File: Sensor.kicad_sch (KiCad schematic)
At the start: 28 parts

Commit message: Add IOT Part
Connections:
- net SPI1_SCLK renamed SPI1_SCK
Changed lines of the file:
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@@
 		)
 	)
-	(label "SPI1_SCLK"
+	(label "SPI1_SCK"
 		(at 163.83 57.15 0)
 		(effects
@@
 		)
 	)
-	(label "SPI1_SCLK"
+	(label "SPI1_SCK"
 		(at 26.67 55.88 0)
 		(effects
@@
 		)
 	)
-	(label "SPI1_SCLK"
+	(label "SPI1_SCK"
 		(at 191.77 135.89 0)
 		(effects

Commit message: IoT part finalization
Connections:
- net SPI1_MISO: no longer U?.1 (SDO/SA0)
- net SPI1_MOSI: no longer U?.14 (SDA)
- net SPI1_SCK: no longer U?.13 (SCL)
- net I2C1_SCL renamed I2C2_SCL
- net I2C1_SDA renamed I2C2_SDA
- new net SPI2_MISO: U?.1 (SDO/SA0)
- new net SPI2_MOSI: U?.14 (SDA)
- new net SPI2_SCK: U?.13 (SCL)

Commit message: IOT part Finilization
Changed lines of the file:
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@@
 	)
 	(junction
-		(at 48.26 35.56)
+		(at 46.99 44.45)
 		(diameter 0)
 		(color 0 0 0 0)
@@
 	)
 	(bus_entry
-		(at 48.26 46.99)
+		(at 46.99 55.88)
 		(size -2.54 2.54)
 		(stroke
 			(width 0)
 			(type default)
+			(color 0 0 132 1)
 		)
 	)
 	(bus_entry
-		(at 48.26 49.53)
+		(at 46.99 58.42)
 		(size 2.54 2.54)
 		(stroke
 			(width 0)
 			(type default)
+			(color 0 0 132 1)
 		)
 	)
 	(bus_entry
-		(at 48.26 54.61)
+		(at 46.99 63.5)
 		(size -2.54 2.54)
 		(stroke
 			(width 0)
 			(type default)
+			(color 0 0 132 1)
 		)
 	)
 	(bus_entry
-		(at 48.26 46.99)
+		(at 46.99 55.88)
 		(size 2.54 2.54)
 		(stroke
 			(width 0)
 			(type default)
+			(color 0 0 132 1)
 		)
 	)
 	(bus_entry
-		(at 48.26 40.64)
+		(at 46.99 49.53)
 		(size -2.54 2.54)
 		(stroke
 			(width 0)
 			(type default)
+			(color 0 0 132 1)
 		)
 	)
 	(bus_entry
-		(at 48.26 52.07)
+		(at 46.99 60.96)
 		(size 2.54 2.54)
 		(stroke
 			(width 0)
 			(type default)
+			(color 0 0 132 1)
 		)
 	)
 	(bus_entry
-		(at 48.26 49.53)
+		(at 46.99 58.42)
 		(size -2.54 2.54)
 		(stroke
 			(width 0)
 			(type default)
+			(color 0 0 132 1)
 		)
 	)
 	(bus_entry
-		(at 48.26 52.07)
+		(at 46.99 60.96)
 		(size -2.54 2.54)
 		(stroke
 			(width 0)
 			(type default)
+			(color 0 0 132 1)
 		)
 	)
 	(bus_entry
-		(at 48.26 54.61)
+		(at 46.99 63.5)
 		(size 2.54 2.54)
 		(stroke
 			(width 0)
 			(type default)
+			(color 0 0 132 1)
 		)
 	)
 	(bus_entry
-		(at 48.26 38.1)
+		(at 46.99 46.99)
 		(size -2.54 2.54)
 		(stroke
 			(width 0)
 			(type default)
+			(color 0 0 132 1)
 		)
 	)
@@
 	(wire
 		(pts
-			(xy 26.67 43.18) (xy 45.72 43.18)
+			(xy 25.4 52.07) (xy 44.45 52.07)
 		)
 		(stroke
@@
 		)
 	)
+	(bus
+		(pts
+			(xy 46.99 43.18) (xy 64.77 43.18)
+		)
+		(stroke
+			(width 0)
+			(type default)
+		)
+	)
 	(wire
 		(pts
@@
 	(wire
 		(pts
-			(xy 26.67 40.64) (xy 45.72 40.64)
+			(xy 25.4 49.53) (xy 44.45 49.53)
 		)
 		(stroke
@@
 	(bus
 		(pts
-			(xy 46.99 35.56) (xy 48.26 35.56)
+			(xy 45.72 44.45) (xy 46.99 44.45)
 		)
 		(stroke
@@
 	(wire
 		(pts
-			(xy 69.85 57.15) (xy 50.8 57.15)
+			(xy 68.58 66.04) (xy 49.53 66.04)
 		)
 		(stroke
@@
 	(wire
 		(pts
-			(xy 69.85 54.61) (xy 50.8 54.61)
+			(xy 68.58 63.5) (xy 49.53 63.5)
 		)
 		(stroke
@@
 	(bus
 		(pts
-			(xy 48.26 34.29) (xy 48.26 35.56)
+			(xy 46.99 43.18) (xy 46.99 44.45)
 		)
 		(stroke
-			(width 0)
+			(width 0.762)
 			(type default)
 		)
@@
 	(wire
 		(pts
-			(xy 26.67 49.53) (xy 45.72 49.53)
-		)
-		(stroke
-			(width 0)
-			(type default)
-		)
-	)
-	(bus
-		(pts
-			(xy 48.26 34.29) (xy 72.39 34.29)
+			(xy 25.4 58.42) (xy 44.45 58.42)
 		)
 		(stroke
@@
 	(bus
 		(pts
-			(xy 48.26 35.56) (xy 48.26 57.15)
+			(xy 46.99 44.45) (xy 46.99 66.04)
 		)
 		(stroke
-			(width 0)
+			(width 0.762)
 			(type default)
 		)
@@
 	(wire
 		(pts
-			(xy 26.67 57.15) (xy 45.72 57.15)
+			(xy 25.4 66.04) (xy 44.45 66.04)
 		)
 		(stroke
@@
 	(wire
 		(pts
-			(xy 26.67 54.61) (xy 45.72 54.61)
+			(xy 25.4 63.5) (xy 44.45 63.5)
 		)
 		(stroke
@@
 	(wire
 		(pts
-			(xy 69.85 52.07) (xy 50.8 52.07)
+			(xy 68.58 60.96) (xy 49.53 60.96)
 		)
 		(stroke
@@
 	(wire
 		(pts
-			(xy 69.85 49.53) (xy 50.8 49.53)
+			(xy 68.58 58.42) (xy 49.53 58.42)
 		)
 		(stroke
@@
 	(wire
 		(pts
-			(xy 26.67 52.07) (xy 45.72 52.07)
+			(xy 25.4 60.96) (xy 44.45 60.96)
 		)
 		(stroke
@@
 	)
 	(label "SPI2_MOSI"
-		(at 69.85 52.07 180)
+		(at 68.58 60.96 180)
 		(effects
 			(font
@@
 	)
 	(label "SPI2_MISO"
-		(at 69.85 54.61 180)
+		(at 68.58 63.5 180)
 		(effects
 			(font
@@
 	)
 	(label "SPI2_CS"
-		(at 69.85 57.15 180)
+		(at 68.58 66.04 180)
 		(effects
 			(font
@@
 	)
 	(label "SPI2_SCK"
-		(at 69.85 49.53 180)
+		(at 68.58 58.42 180)
 		(effects
 			(font
@@
 	)
 	(label "SPI1_SCK"
-		(at 26.67 49.53 0)
+		(at 25.4 58.42 0)
 		(effects
 			(font
@@
 	)
 	(label "{MCU_Serial_COM}"
-		(at 52.07 34.29 0)
+		(at 46.99 43.18 0)
 		(effects
 			(font
@@
 	)
 	(label "SPI1_CS"
-		(at 26.67 57.15 0)
+		(at 25.4 66.04 0)
 		(effects
 			(font
@@
 	)
 	(label "SPI1_MOSI"
-		(at 26.67 52.07 0)
+		(at 25.4 60.96 0)
 		(effects
 			(font
@@
 	)
 	(label "I2C2_SCL"
-		(at 26.67 43.18 0)
+		(at 25.4 52.07 0)
 		(effects
 			(font
@@
 	)
 	(label "SPI1_MISO"
-		(at 26.67 54.61 0)
+		(at 25.4 63.5 0)
 		(effects
 			(font
@@
 	)
 	(label "I2C2_SDA"
-		(at 26.67 40.64 0)
+		(at 25.4 49.53 0)
 		(effects
 			(font
@@
 	(hierarchical_label "{MCU_Serial_COM}"
 		(shape bidirectional)
-		(at 46.99 35.56 180)
+		(at 45.72 44.45 180)
 		(effects
 			(font
@@
 				(font
 					(size 1.27 1.27)
+					(color 132 0 0 1)
 				)
 			)
@@
 				(font
 					(size 1.27 1.27)
+					(color 132 0 0 1)
 				)
 			)
@@
 				(font
 					(size 1.27 1.27)
+					(color 132 0 0 1)
 				)
 			)
@@
 				(font
 					(size 1.27 1.27)
+					(color 132 0 0 1)
 				)
 			)
@@
 				(font
 					(size 1.27 1.27)
+					(color 132 0 0 1)
 				)
 			)
@@
 				(font
 					(size 1.27 1.27)
+					(color 132 0 0 1)
 				)
 			)
@@
 				(font
 					(size 1.27 1.27)
+					(color 132 0 0 1)
 				)
 			)
@@
 				(font
 					(size 1.27 1.27)
+					(color 132 0 0 1)
 				)
 			)
@@
 				(font
 					(size 1.27 1.27)
+					(color 132 0 0 1)
 				)
 			)
@@
 				(font
 					(size 1.27 1.27)
+					(color 132 0 0 1)
 				)
 			)
@@
 				(font
 					(size 1.27 1.27)
+					(color 132 0 0 1)
 				)
 			)
@@
 				(font
 					(size 1.27 1.27)
+					(color 132 0 0 1)
 				)
 			)

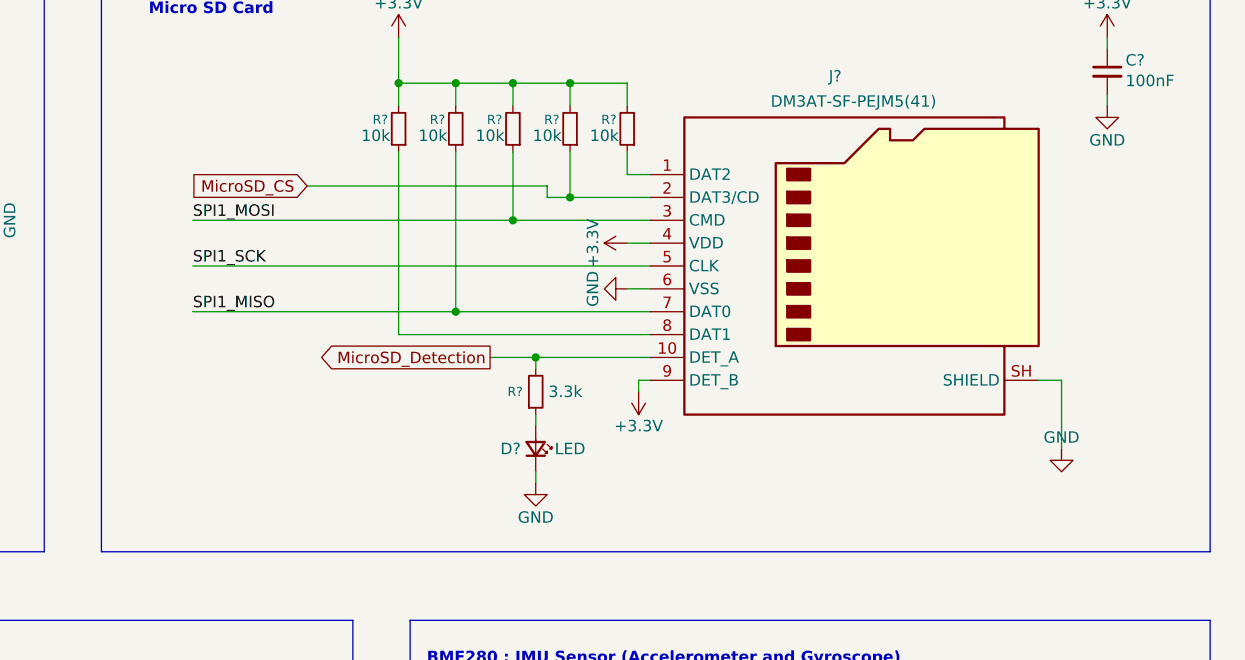
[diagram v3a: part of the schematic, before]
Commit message: Add power part : LDO and SMPS regulators
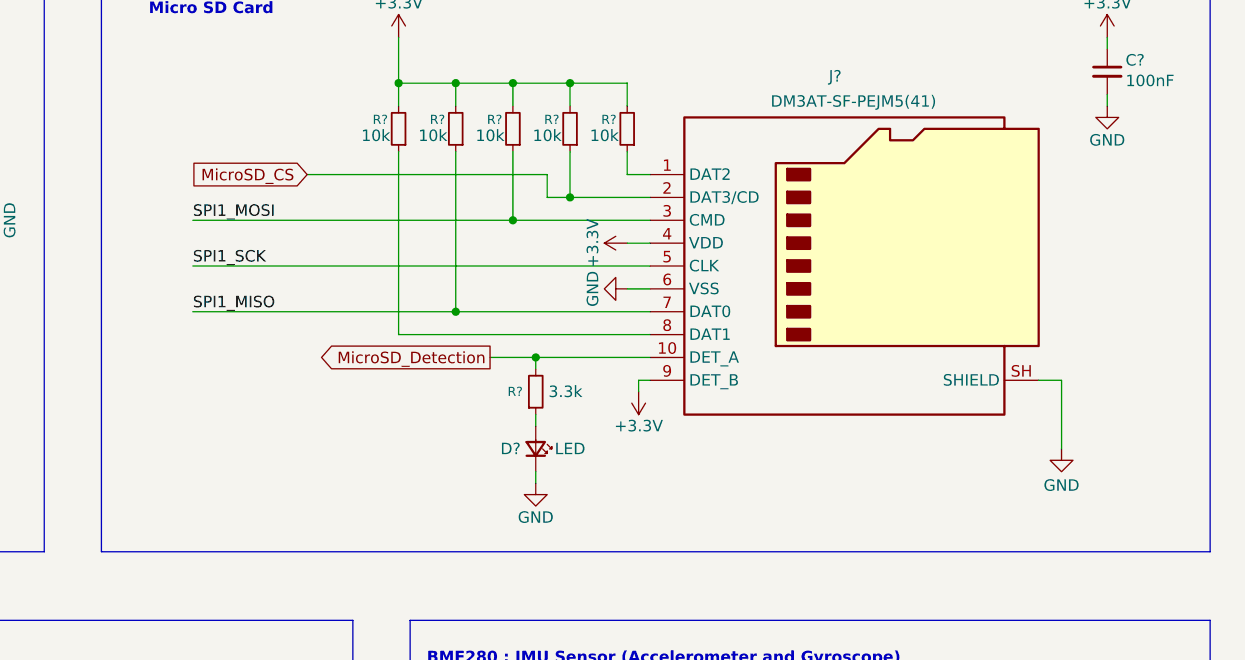
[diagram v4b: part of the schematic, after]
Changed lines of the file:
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@@
 	(wire
 		(pts
-			(xy 203.2 48.26) (xy 203.2 49.53)
+			(xy 203.2 46.99) (xy 203.2 49.53)
 		)
 		(stroke
@@
 	(wire
 		(pts
-			(xy 176.53 48.26) (xy 203.2 48.26)
+			(xy 176.53 46.99) (xy 203.2 46.99)
 		)
 		(stroke
@@
 	(global_label "MicroSD_CS"
 		(shape input)
-		(at 176.53 48.26 180)
+		(at 176.53 46.99 180)
 		(fields_autoplaced yes)
 		(effects
@@
 		)
 		(property "Intersheetrefs" "${INTERSHEET_REFS}"
-			(at 162.5382 48.26 0)
+			(at 162.5382 46.99 0)
 			(hide yes)
 			(show_name no)
@@
 		)
 		(property "Value" "GND"
-			(at 260.35 76.2 0)
+			(at 260.35 81.534 0)
 			(show_name no)
 			(do_not_autoplace no)

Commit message: Release Schematic REV A-01
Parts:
- R56: renamed from R?; value 0R -> 1k
- gave numbers to parts that had none: 27
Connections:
- net SPI1_MISO: no longer J27.7 (DAT0), R51.1
- net SPI1_MOSI: no longer J27.3 (CMD), R52.1
- net SPI1_SCK: no longer J27.5 (CLK)
- net MicroSD_CS renamed ESP_SPI_CS0
- new net ESP_SPI_MISO: J27.7 (DAT0), R51.1
- new net ESP_SPI_MOSI: J27.3 (CMD), R52.1
- new net ESP_SPI_SCK: J27.5 (CLK)
- no-connect marks 1 -> 2
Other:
- company: Blue Signal -> Nexvantis
